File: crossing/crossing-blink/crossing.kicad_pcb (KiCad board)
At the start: 2 copper layers, 38 x 66.7 mm, 14 parts, among them Q1 2N3904, Q2 2N3904, SW1 SW_SPDT

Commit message: crossing
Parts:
- SW1: moved to F.Cu
- moved SW1 31.3 mm to (97.5, 154.0)
- moved C1 23.6 mm to (143.0, 146.8), turned to 90 degrees
- moved C2 22.0 mm to (122.5, 137.5), turned to -90 degrees
- moved Q2 20.5 mm to (123.5, 144.0), turned to -67.5 degrees
- moved Q1 20.0 mm to (143.0, 141.0), turned to 90 degrees
- moved R2 18.2 mm to (142.9, 155.9), turned to 65.5 degrees
- moved R3 13.2 mm to (128.6, 155.9), turned to 114.5 degrees
- moved R1 8.27 mm to (123.6, 155.9)
- moved R4 4.98 mm to (137.9, 155.9)
- moved BT1 0.60 mm to (133.2, 115.7)
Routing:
- net Net-(D2-K): track 32.5 -> 0.00 mm
- net Net-(BT1-+): track 32.0 -> 0.00 mm
- net Net-(D1-A): track 25.4 -> 0.00 mm
- net Net-(D2-A): track 25.1 -> 0.00 mm
- net Net-(D1-K): track 24.3 -> 0.00 mm
- net GND: track 5.74 -> 0.00 mm
- net Net-(Q1-B): track 3.11 -> 0.00 mm
- net Net-(Q2-B): track 2.48 -> 0.00 mm

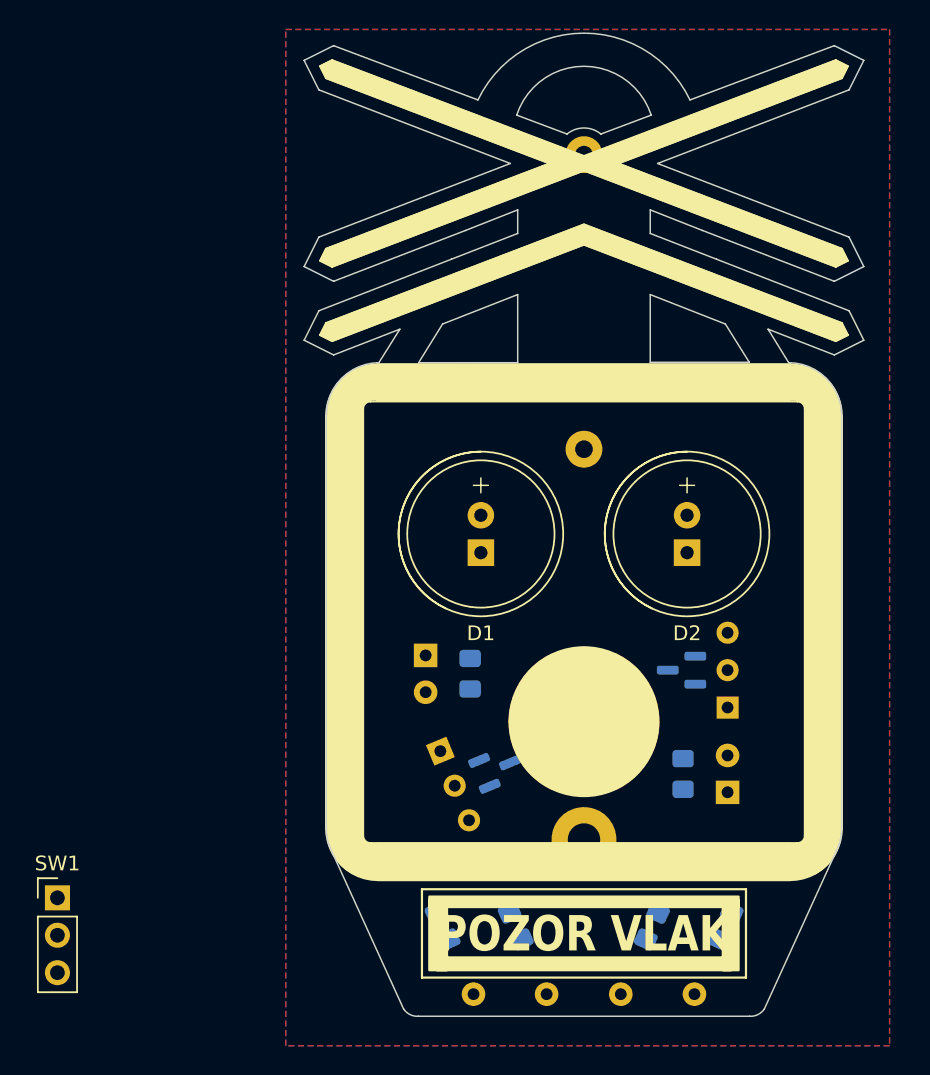
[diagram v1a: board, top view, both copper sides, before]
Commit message: Finished crossing for production, modified other
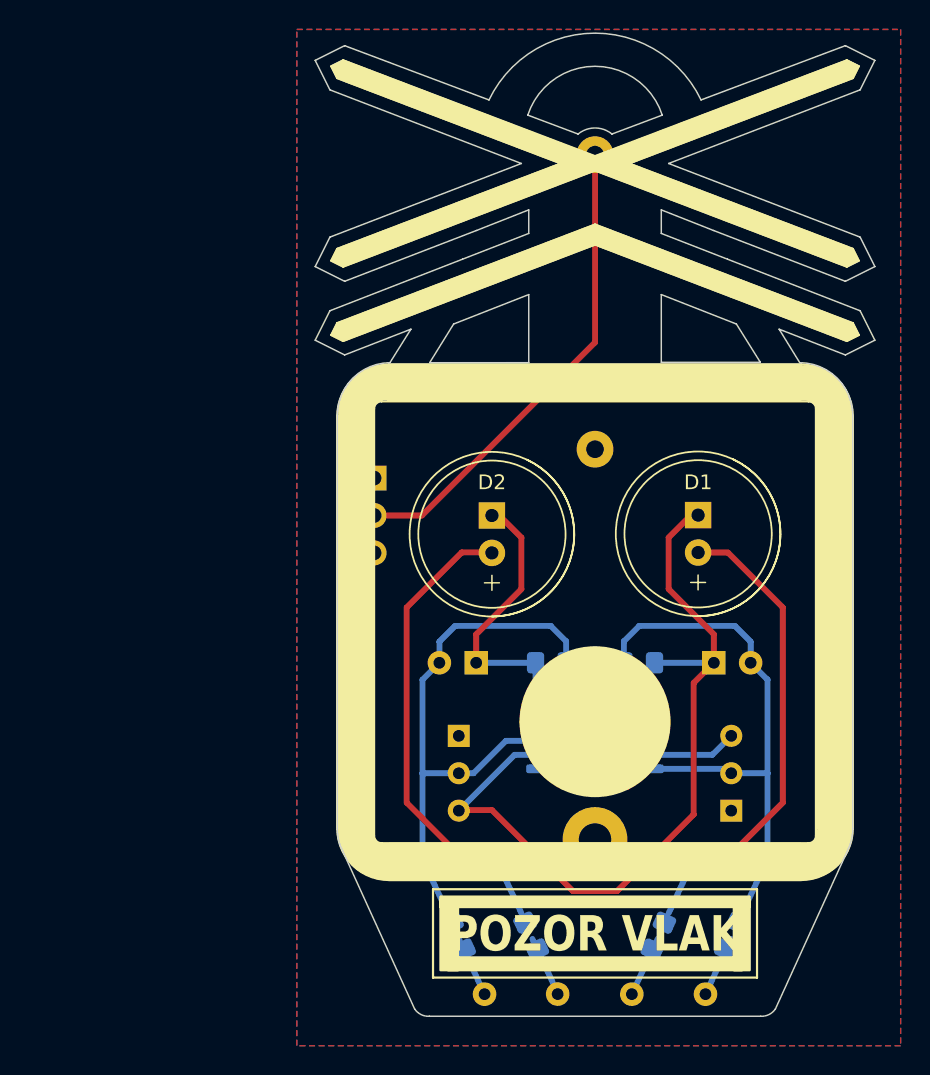
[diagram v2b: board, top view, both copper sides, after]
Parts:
- removed REF**: Touch_pad, lib:Touchpad_resistive
- removed REF**: MountingHole_2.2mm_M2_Pad, MountingHole:MountingHole_2.2mm_M2_Pad
- added C3: 47u, Capacitor_SMD:C_0805_2012Metric_Pad1.18x1.45mm_HandSolder, B.Cu at (137.0, 138.0)
- added C4: 47u, Capacitor_SMD:C_0805_2012Metric_Pad1.18x1.45mm_HandSolder, B.Cu at (131.0, 138.0)
- added H1: MountingHole, MountingHole:MountingHole_2.2mm_M2_Pad, F.Cu at (134.0, 150.0)
- added PAD1: WHITE_PAD, lib:Touchpad_resistive, F.Cu at (134.0, 142.0)
- added Q3: 2N3904, Package_TO_SOT_SMD:SOT-23, B.Cu at (131.0, 144.2)
- added Q4: 2N3904, Package_TO_SOT_SMD:SOT-23, B.Cu at (137.0, 144.2)
- C1, C2: footprint lib:CP_Radial_D6.3mm_P2.50mm+SMD_0805 -> Capacitor_THT:CP_Radial_D6.3mm_P2.50mm
- Q1: renamed from Q2; footprint lib:TO-92L_Inline_Wide+SMD_SOT-23 -> Package_TO_SOT_THT:TO-92L_Inline_Wide
- Q2: renamed from Q1; footprint lib:TO-92L_Inline_Wide+SMD_SOT-23 -> Package_TO_SOT_THT:TO-92L_Inline_Wide
- SW1: moved to B.Cu
- moved SW1 35.7 mm to (119.0, 125.5), turned to 180 degrees
- moved R1 15.0 mm to (138.6, 155.9), turned to 65.5 degrees
- moved C1 8.84 mm to (142.1, 138.0), turned to 0 degrees
- moved R4 8.50 mm to (129.4, 155.9), turned to 114.5 degrees
- moved Q2 7.00 mm to (143.2, 148.0)
- moved R3 4.21 mm to (124.4, 155.9)
- moved C2 3.47 mm to (125.9, 138.0), turned to 180 degrees
- moved D1 2.66 mm to (141.0, 128.0), turned to -90 degrees
- moved D2 2.63 mm to (127.0, 128.0), turned to -90 degrees
- moved Q1 1.63 mm to (124.8, 143.0), turned to -90 degrees
- moved BT1 0.75 mm to (134.0, 115.7)
- moved R2 0.75 mm to (143.6, 155.9)
- renumbered D2 to D1, D1 to D2
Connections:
- C1 pad 1: Net-(D1-K) -> /side_1
- C1 pad 2: Net-(Q2-B) -> /mid_1
- C2 pad 1: Net-(D2-K) -> /side_2
- C2 pad 2: Net-(Q1-B) -> /mid_2
- D1 pad 1: Net-(D2-K) -> /side_1
- D1 pad 2: Net-(D2-A) -> Net-(D1-A)
- D2 pad 1: Net-(D1-K) -> /side_2
- D2 pad 2: Net-(D1-A) -> Net-(D2-A)
- Q1 pad 2: Net-(Q2-B) -> /mid_2
- Q1 pad 3: Net-(D2-K) -> /side_1
- Q2 pad 2: Net-(Q1-B) -> /mid_1
- Q2 pad 3: Net-(D1-K) -> /side_2
- R2 pad 2: Net-(Q2-B) -> /mid_1
- R3 pad 2: Net-(Q1-B) -> /mid_2
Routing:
- net /side_1: track 0.00 -> 56.5 mm
- net /side_2: track 0.00 -> 35.0 mm
- net /mid_2: track 0.00 -> 34.8 mm
- net /mid_1: track 0.00 -> 34.0 mm
- net Net-(BT1-+): track 0.00 -> 32.6 mm
- net Net-(D1-A): track 0.00 -> 28.1 mm
- net Net-(D2-A): track 0.00 -> 28.1 mm
- added copper zone on F.Cu, net +3.3V
- added copper zone on B.Cu, net GND
- removed copper zone on B.Cu, net +3.3V
- removed copper zone on F.Cu, net GND
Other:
- board size 38 x 66.7 mm -> 38 x 66.8 mm
- board text removed: "1"
- board text removed: "10k"
- board text removed: "1M"
- board text removed: "2"
- board text removed: "47u"

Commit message: boom prask netopyr netopyr
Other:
- board text added: "V2.0"
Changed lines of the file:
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@@
 		(tags "TO-92L Inline Wide transistor")
 		(property "Reference" "Q1"
-			(at 3.79 -6.25 0)
+			(at 4.29 -6.25 0)
 			(layer "B.SilkS")
 			(effects
@@
 		(tags "TO-92L Inline Wide transistor")
 		(property "Reference" "Q2"
-			(at 1.289999 -6.25 180)
+			(at 0.789999 -6.25 180)
 			(layer "B.SilkS")
 			(effects
@@
 	)
 	(gr_line
-		(start 129 147.25)
-		(end 128.5 146.75)
+		(start 129 147.75)
+		(end 128.5 147.25)
 		(stroke
 			(width 0.15)
@@
 	)
 	(gr_line
-		(start 128.5 146.75)
-		(end 129 146.25)
+		(start 128.5 147.25)
+		(end 129 146.75)
 		(stroke
 			(width 0.15)
@@
 	)
 	(gr_line
-		(start 129.5 146.75)
-		(end 128.5 146.75)
+		(start 129.5 147.25)
+		(end 128.5 147.25)
 		(stroke
 			(width 0.15)
@@
 	)
 	(gr_line
-		(start 139.5 146.75)
-		(end 139 147.25)
+		(start 139.5 147.25)
+		(end 139 147.75)
 		(stroke
 			(width 0.15)
@@
 	)
 	(gr_line
-		(start 139 146.25)
-		(end 139.5 146.75)
+		(start 139 146.75)
+		(end 139.5 147.25)
 		(stroke
 			(width 0.15)
@@
 	)
 	(gr_line
-		(start 138.5 146.75)
-		(end 139.5 146.75)
+		(start 138.5 147.25)
+		(end 139.5 147.25)
 		(stroke
 			(width 0.15)
@@
 	)
 	(gr_text "pajecistavebnice.cz"
-		(at 150.25 130.25 90)
+		(at 150.25 121.250002 90)
 		(layer "B.SilkS")
 		(effects
@@
 				(thickness 0.15)
 			)
-			(justify bottom mirror)
+			(justify left bottom mirror)
 		)
 	)
@@
 		(layer "B.SilkS")
 		(effects
+			(font
+				(size 1 1)
+				(thickness 0.15)
+			)
+			(justify mirror)
+		)
+	)
+	(gr_text "V2.0"
+		(at 121.5 158.25 -65)
+		(layer "B.SilkS")
+		(effects

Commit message: Crossing V2.1
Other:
- board text added: "V2.1"
- board text removed: "100"
- board text removed: "62k"
- board text removed: "V2.0"
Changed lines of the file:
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@@
 		)
 		(fp_line
-			(start -0.518936 -0.735)
-			(end -0.973064 -0.735)
+			(start 0.227064 -0.72)
+			(end -0.227064 -0.72)
 			(stroke
 				(width 0.12)
@@
 		)
 		(fp_line
-			(start -0.518936 0.735)
-			(end -0.973064 0.735)
+			(start 0.227064 0.75)
+			(end -0.227065 0.75)
 			(stroke
 				(width 0.12)
@@
 		)
 		(fp_line
-			(start 1.104 -0.95)
-			(end 1.104 0.95)
+			(start 1.85 -0.935)
+			(end 1.85 0.965)
 			(stroke
 				(width 0.05)
@@
 		)
 		(fp_line
-			(start -2.596 -0.95)
-			(end 1.104 -0.95)
+			(start -1.850001 -0.935)
+			(end 1.85 -0.935)
 			(stroke
 				(width 0.05)
@@
 		)
 		(fp_line
-			(start 1.104 0.95)
-			(end -2.596 0.95)
+			(start 1.85 0.965)
+			(end -1.85 0.965)
 			(stroke
 				(width 0.05)
@@
 		)
 		(fp_line
-			(start -2.596 0.95)
-			(end -2.596 -0.95)
+			(start -1.85 0.965)
+			(end -1.850001 -0.935)
 			(stroke
 				(width 0.05)
@@
 		)
 		(pad "1" smd roundrect
-			(at -1.745999 0 114.5)
+			(at -1 0.015 114.5)
 			(size 1.2 1.4)
 			(layers "B.Cu" "B.Paste" "B.Mask")
@@
 		)
 		(pad "2" smd roundrect
-			(at 0.254 0 114.5)
+			(at 1 0.015 114.5)
 			(size 1.2 1.4)
 			(layers "B.Cu" "B.Paste" "B.Mask")
@@
 		)
 		(fp_line
-			(start -0.518936 -0.735)
-			(end -0.973064 -0.735)
+			(start 0.227064 -0.72)
+			(end -0.227064 -0.72)
 			(stroke
 				(width 0.12)
@@
 		)
 		(fp_line
-			(start -0.518936 0.735)
-			(end -0.973064 0.735)
+			(start 0.227065 0.75)
+			(end -0.227064 0.75)
 			(stroke
 				(width 0.12)
@@
 		)
 		(fp_line
-			(start -2.596 -0.95)
-			(end 1.104 -0.95)
+			(start -1.85 -0.935)
+			(end 1.850001 -0.935)
 			(stroke
 				(width 0.05)
@@
 		)
 		(fp_line
-			(start 1.104 -0.95)
-			(end 1.104 0.95)
+			(start 1.850001 -0.935)
+			(end 1.85 0.965)
 			(stroke
 				(width 0.05)
@@
 		)
 		(fp_line
-			(start -2.596 0.95)
-			(end -2.596 -0.95)
+			(start -1.85 0.965)
+			(end -1.85 -0.935)
 			(stroke
 				(width 0.05)
@@
 		)
 		(fp_line
-			(start 1.104 0.95)
-			(end -2.596 0.95)
+			(start 1.85 0.965)
+			(end -1.85 0.965)
 			(stroke
 				(width 0.05)
@@
 		)
 		(pad "1" smd roundrect
-			(at -1.745999 0 65.5)
+			(at -1 0.015 65.5)
 			(size 1.2 1.4)
 			(layers "B.Cu" "B.Paste" "B.Mask")
@@
 		)
 		(pad "2" smd roundrect
-			(at 0.254 0 65.5)
+			(at 1 0.015 65.5)
 			(size 1.2 1.4)
 			(layers "B.Cu" "B.Paste" "B.Mask")
@@
 		)
 		(fp_line
-			(start -0.518936 -0.735)
-			(end -0.973064 -0.735)
+			(start 0.227064 -0.72)
+			(end -0.227064 -0.72)
 			(stroke
 				(width 0.12)
@@
 		)
 		(fp_line
-			(start -0.518936 0.735)
-			(end -0.973064 0.735)
+			(start 0.227065 0.75)
+			(end -0.227064 0.75)
 			(stroke
 				(width 0.12)
@@
 		)
 		(fp_line
-			(start -2.596 -0.95)
-			(end 1.104 -0.95)
+			(start -1.85 -0.935)
+			(end 1.850001 -0.935)
 			(stroke
 				(width 0.05)
@@
 		)
 		(fp_line
-			(start 1.104 -0.95)
-			(end 1.104 0.95)
+			(start 1.850001 -0.935)
+			(end 1.85 0.965)
 			(stroke
 				(width 0.05)
@@
 		)
 		(fp_line
-			(start -2.596 0.95)
-			(end -2.596 -0.95)
+			(start -1.85 0.965)
+			(end -1.85 -0.935)
 			(stroke
 				(width 0.05)
@@
 		)
 		(fp_line
-			(start 1.104 0.95)
-			(end -2.596 0.95)
+			(start 1.85 0.965)
+			(end -1.85 0.965)
 			(stroke
 				(width 0.05)
@@
 		)
 		(pad "1" smd roundrect
-			(at -1.745999 0 65.5)
+			(at -1 0.015 65.5)
 			(size 1.2 1.4)
 			(layers "B.Cu" "B.Paste" "B.Mask")
@@
 		)
 		(pad "2" smd roundrect
-			(at 0.254 0 65.5)
+			(at 1 0.015 65.5)
 			(size 1.2 1.4)
 			(layers "B.Cu" "B.Paste" "B.Mask")
@@
 		)
 		(fp_line
-			(start -0.518936 -0.735)
-			(end -0.973064 -0.735)
+			(start 0.227064 -0.72)
+			(end -0.227064 -0.72)
 			(stroke
 				(width 0.12)
@@
 		)
 		(fp_line
-			(start -0.518936 0.735)
-			(end -0.973064 0.735)
+			(start 0.227064 0.75)
+			(end -0.227065 0.75)
 			(stroke
 				(width 0.12)
@@
 		)
 		(fp_line
-			(start 1.104 -0.95)
-			(end 1.104 0.95)
+			(start 1.85 -0.935)
+			(end 1.85 0.965)
 			(stroke
 				(width 0.05)
@@
 		)
 		(fp_line
-			(start -2.596 -0.95)
-			(end 1.104 -0.95)
+			(start -1.850001 -0.935)
+			(end 1.85 -0.935)
 			(stroke
 				(width 0.05)
@@
 		)
 		(fp_line
-			(start 1.104 0.95)
-			(end -2.596 0.95)
+			(start 1.85 0.965)
+			(end -1.85 0.965)
 			(stroke
 				(width 0.05)
@@
 		)
 		(fp_line
-			(start -2.596 0.95)
-			(end -2.596 -0.95)
+			(start -1.85 0.965)
+			(end -1.850001 -0.935)
 			(stroke
 				(width 0.05)
@@
 		)
 		(pad "1" smd roundrect
-			(at -1.745999 0 114.5)
+			(at -1 0.015 114.5)
 			(size 1.2 1.4)
 			(layers "B.Cu" "B.Paste" "B.Mask")
@@
 		)
 		(pad "2" smd roundrect
-			(at 0.254 0 114.5)
+			(at 1 0.015 114.5)
 			(size 1.2 1.4)
 			(layers "B.Cu" "B.Paste" "B.Mask")
@@
 		(layer "F.SilkS")
 	)
-	(gr_circle
-		(center 134 142)
-		(end 139 142)
-		(stroke
-			(width 0.15)
-			(type solid)
-		)
-		(fill solid)
-		(layer "F.SilkS")
-	)
 	(gr_poly
 		(pts
@@
 		(layer "Edge.Cuts")
 	)
-	(gr_text "100"
-		(at 128.461318 153.907997 24.5)
-		(layer "B.SilkS")
-		(effects
-			(font
-				(size 1 1)
-				(thickness 0.15)
-			)
-			(justify mirror)
-		)
-	)
-	(gr_text "OFF"
+	(gr_text "ON"
 		(at 125 126.5 0)
 		(layer "B.SilkS")
@@
 		)
 	)
-	(gr_text "62k"
-		(at 144.501965 153.912791 335.5)
-		(layer "B.SilkS")
-		(effects
-			(font
-				(size 1 1)
-				(thickness 0.15)
-			)
-			(justify mirror)
-		)
-	)
-	(gr_text "62k"
-		(at 123.498035 153.912791 24.5)
-		(layer "B.SilkS")
-		(effects
-			(font
-				(size 1 1)
-				(thickness 0.15)
-			)
-			(justify mirror)
-		)
-	)
 	(gr_text "pajecistavebnice.cz"
 		(at 150.25 121.250002 90)
@@
 		)
 	)
-	(gr_text "100"
-		(at 139.501964 153.912791 335.5)
-		(layer "B.SilkS")
-		(effects
-			(font
-				(size 1 1)
-				(thickness 0.15)
-			)
-			(justify mirror)
-		)
-	)
-	(gr_text "V2.0"
-		(at 121.5 158.25 -65)
+	(gr_text "V2.1"
+		(at 121.5 158.25 295)
 		(layer "B.SilkS")
 		(effects
@@
 		)
 	)
-	(gr_text "ON"
+	(gr_text "OFF"
 		(at 125 129.5 0)
 		(layer "B.SilkS")
